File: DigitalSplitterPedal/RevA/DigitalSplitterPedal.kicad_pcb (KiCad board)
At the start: 2 copper layers, 112.5 x 86.4 mm, 84 parts, among them J1 MonoJack2Switch, J2 Barrel_Jack, J3 MonoJack2Switch, J4 MonoJack2Switch, J5 MonoJack2Switch, J6 MonoJack2Switch, J7 Conn_01x05, U1 MCP1703A-3302_SOT223, U10 MCP601-xOT, U11 TL072, U13 TPS60400, U14 TPS60400, U15 TPS60400, U16 MCP601-xOT, U17 MCP601-xOT, U2 TL072, U3 TPS60400, U4 STM32F051K8Tx, U5 TL072, U7 MCP601-xOT, U8 TL072

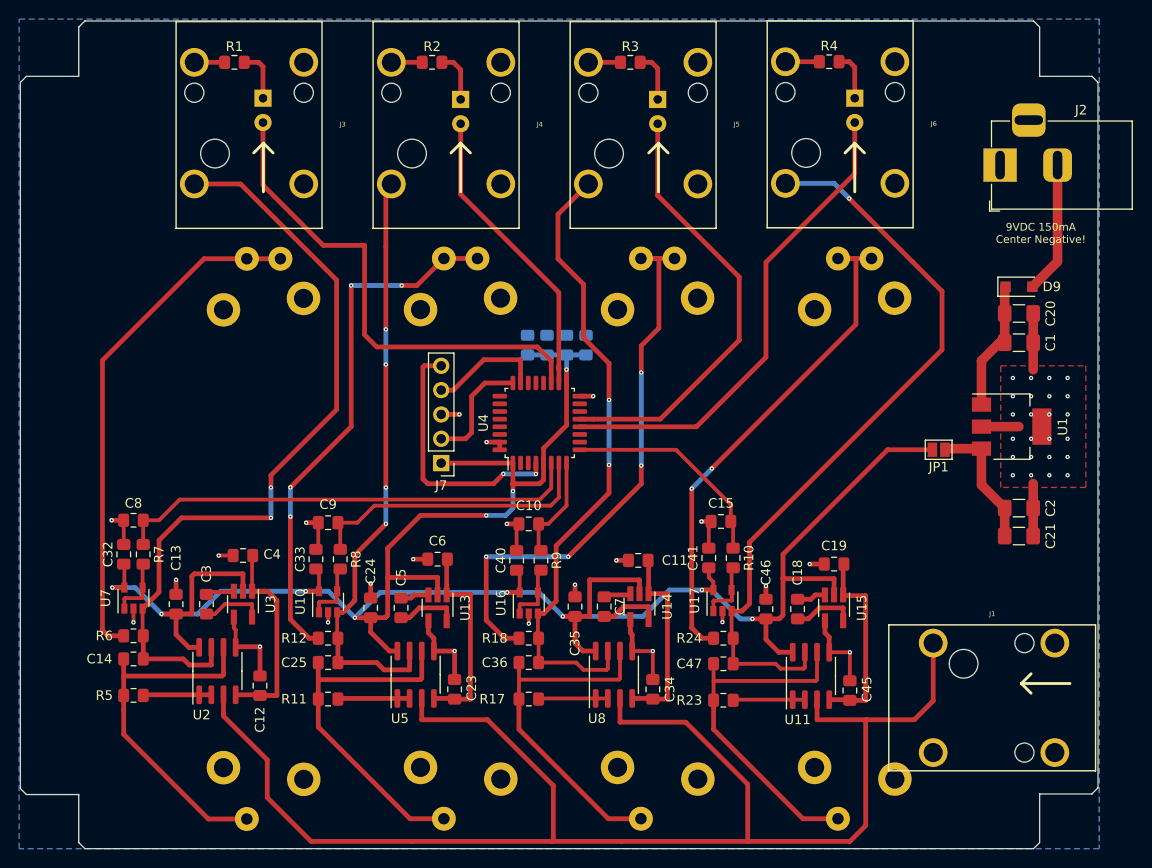
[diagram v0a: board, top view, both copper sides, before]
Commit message: updated hw
- add testpoints
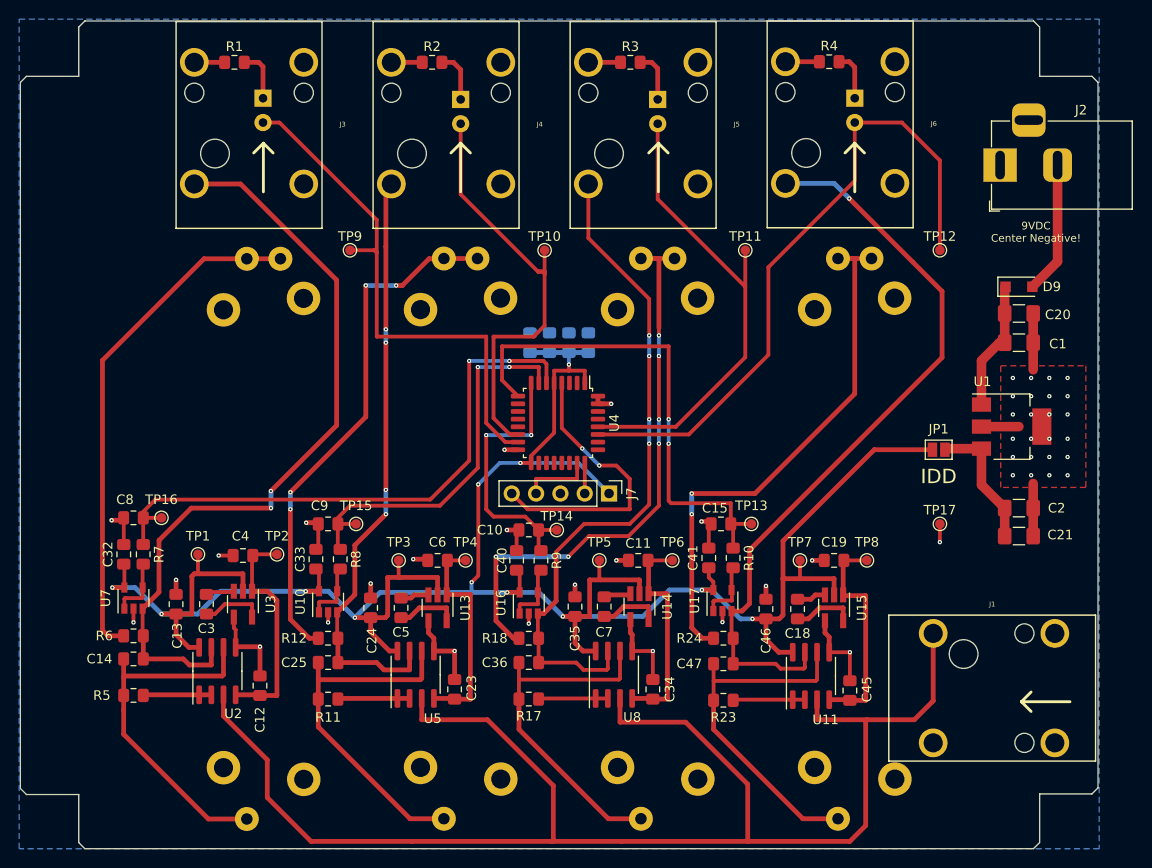
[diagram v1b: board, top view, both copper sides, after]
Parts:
- added TP1: TestPoint, TestPoint:TestPoint_Pad_D1.0mm, F.Cu at (98.4, 100.3)
- added TP10: TestPoint, TestPoint:TestPoint_Pad_D1.0mm, F.Cu at (134.6, 68.6)
- added TP11: TestPoint, TestPoint:TestPoint_Pad_D1.0mm, F.Cu at (155.6, 68.6)
- added TP12: TestPoint, TestPoint:TestPoint_Pad_D1.0mm, F.Cu at (175.9, 68.6)
- added TP13: TestPoint, TestPoint:TestPoint_Pad_D1.0mm, F.Cu at (156.2, 97.2)
- added TP14: TestPoint, TestPoint:TestPoint_Pad_D1.0mm, F.Cu at (135.9, 97.8)
- added TP15: TestPoint, TestPoint:TestPoint_Pad_D1.0mm, F.Cu at (114.9, 97.2)
- added TP16: TestPoint, TestPoint:TestPoint_Pad_D1.0mm, F.Cu at (94.6, 96.5)
- added TP17: TestPoint, TestPoint:TestPoint_Pad_D1.0mm, F.Cu at (175.9, 97.2)
- added TP2: TestPoint, TestPoint:TestPoint_Pad_D1.0mm, F.Cu at (106.7, 100.3)
- added TP3: TestPoint, TestPoint:TestPoint_Pad_D1.0mm, F.Cu at (119.4, 101.0)
- added TP4: TestPoint, TestPoint:TestPoint_Pad_D1.0mm, F.Cu at (126.4, 101.0)
- added TP5: TestPoint, TestPoint:TestPoint_Pad_D1.0mm, F.Cu at (140.3, 101.0)
- added TP6: TestPoint, TestPoint:TestPoint_Pad_D1.0mm, F.Cu at (148.0, 101.0)
- added TP7: TestPoint, TestPoint:TestPoint_Pad_D1.0mm, F.Cu at (161.3, 101.0)
- added TP8: TestPoint, TestPoint:TestPoint_Pad_D1.0mm, F.Cu at (168.3, 101.0)
- added TP9: TestPoint, TestPoint:TestPoint_Pad_D1.0mm, F.Cu at (114.3, 68.6)
- moved J7 17.8 mm to (141.4, 94.0), turned to 270 degrees
- moved U4 1.91 mm to (136.0, 86.6), turned to 270 degrees
- moved J1 1.02 mm to (181.4, 114.3)
- moved C10 0.64 mm to (133.0, 97.8)
- moved C19 0.38 mm to (164.8, 101.0)
- moved C30 0.36 mm to (139.2, 78.2)
- moved C22 0.36 mm to (133.1, 78.2)
- moved C29 0.36 mm to (135.1, 78.2)
- moved C31 0.36 mm to (137.2, 78.2)
- moved C15 0.25 mm to (153.0, 97.2)
- moved C8 0.25 mm to (91.7, 96.5)
- moved C6 0.13 mm to (123.4, 101.0)
- moved C9 0.13 mm to (112.0, 97.2)
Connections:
- J3 pad 2: Net-(J3-Pad2) -> GNDS
- J4 pad 2: Net-(J4-Pad2) -> GNDS
- J5 pad 2: Net-(J5-Pad2) -> GNDS
- J6 pad 2: Net-(J6-Pad2) -> GNDS
- U4 pad 12: /PeakDetectorMCU/PEAK_OUT_PWM1 -> Net-(U4-Pad12)
- U4 pad 13: /PeakDetectorMCU/PEAK_OUT_PWM2 -> Net-(U4-Pad13)
- U4 pad 14: Net-(U4-Pad14) -> /PeakDetectorMCU/PEAK_OUT_PWM3
- U4 pad 15: Net-(U4-Pad15) -> /PeakDetectorMCU/PEAK_OUT_PWM4
- U4 pad 18: /PeakDetectorMCU/PEAK_OUT_PWM3 -> Net-(U4-Pad18)
- U4 pad 19: /PeakDetectorMCU/PEAK_OUT_PWM4 -> Net-(U4-Pad19)
- U4 pad 27: Net-(U4-Pad27) -> /PeakDetectorMCU/PEAK_OUT_PWM1
- U4 pad 28: Net-(U4-Pad28) -> /PeakDetectorMCU/PEAK_OUT_PWM2
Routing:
- net /PeakDetectorMCU/PEAK_IN_ADC4: track 22.8 -> 53.0 mm, vias 0 -> 2
- net /PeakDetectorMCU/PEAK_OUT_PWM1: track 50.8 -> 69.1 mm
- net /PeakDetectorMCU/PEAK_IN_ADC3: track 11.1 -> 28.4 mm, vias 0 -> 2
- net /PeakDetectorMCU/PEAK_OUT_PWM3: track 31.6 -> 45.6 mm
- net /PeakDetectorMCU/PEAK_IN_ADC1: track 49.1 -> 62.2 mm, vias 0 -> 2
- net /PeakDetectorMCU/PEAK_IN_ADC2: track 30.7 -> 40.8 mm, vias 0 -> 2
- net /PeakDetectorMCU/SYS_SWCLK: track 12.1 -> 3.19 mm
- net +3V3: track 243.4 -> 250.9 mm, vias 11 -> 12
- net /PeakDetectorMCU/SYS_SWDIO: track 12.0 -> 7.46 mm
- net /PeakDetectorMCU/PEAK_OUT_PWM2: track 46.2 -> 50.4 mm
- net Net-(R24-Pad2): track 53.7 -> 57.5 mm
- net /PeakDetectorMCU/PEAK_OUT_PWM4: track 52.0 -> 55.8 mm
- net /PEAK_IN_BUF3: track 66.5 -> 70.1 mm, vias 2 -> 4
- net /PeakDetectorMCU/NRST: track 27.2 -> 30.2 mm
- net /InputBufferAndGain1/NEGVIN: track 21.0 -> 23.6 mm
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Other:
- board text added: "4-Way Spliiter with Digital Peak Detect RevA 3920"
- board text added: "9VDC Center Negative!"
- board text added: "IDD"
- board text removed: "9VDC 150mA Center Negative!"
- board text removed: "Active 4-Way Splitter RevD 3720"
